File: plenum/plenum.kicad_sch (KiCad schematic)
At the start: 4 parts

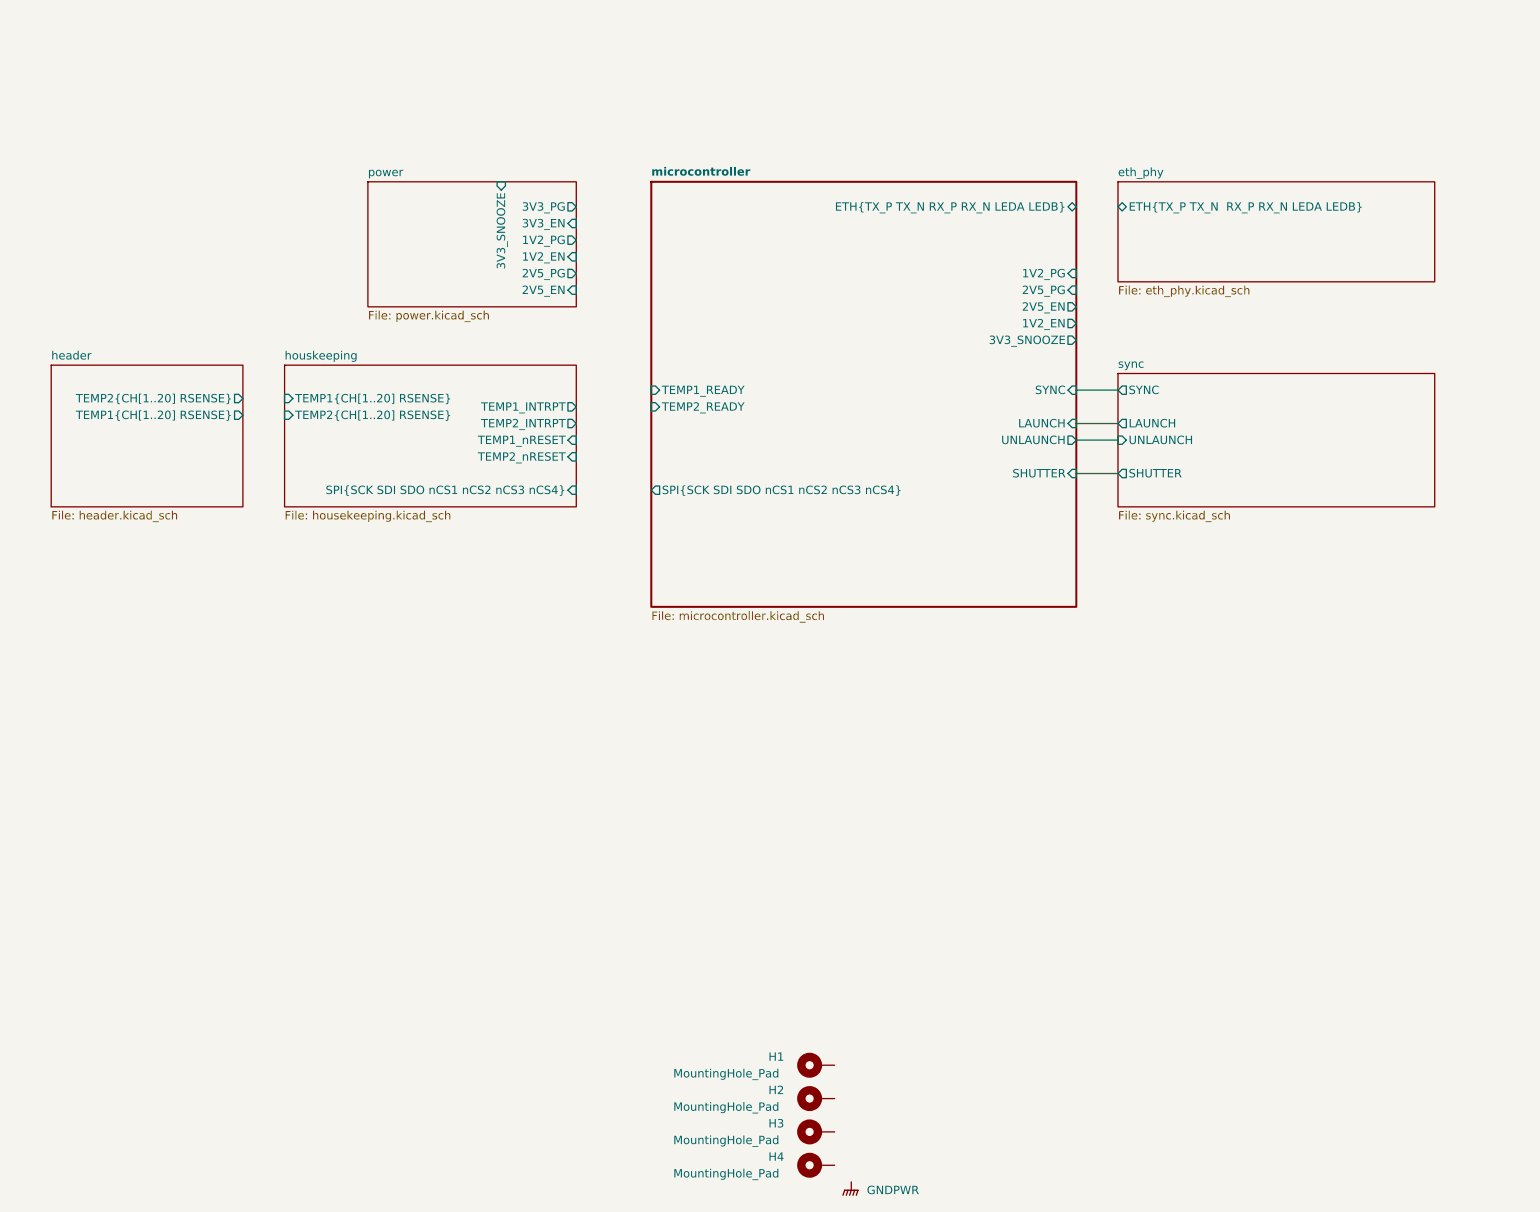
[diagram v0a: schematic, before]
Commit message: adding notes and BMI270 IMU to plenum
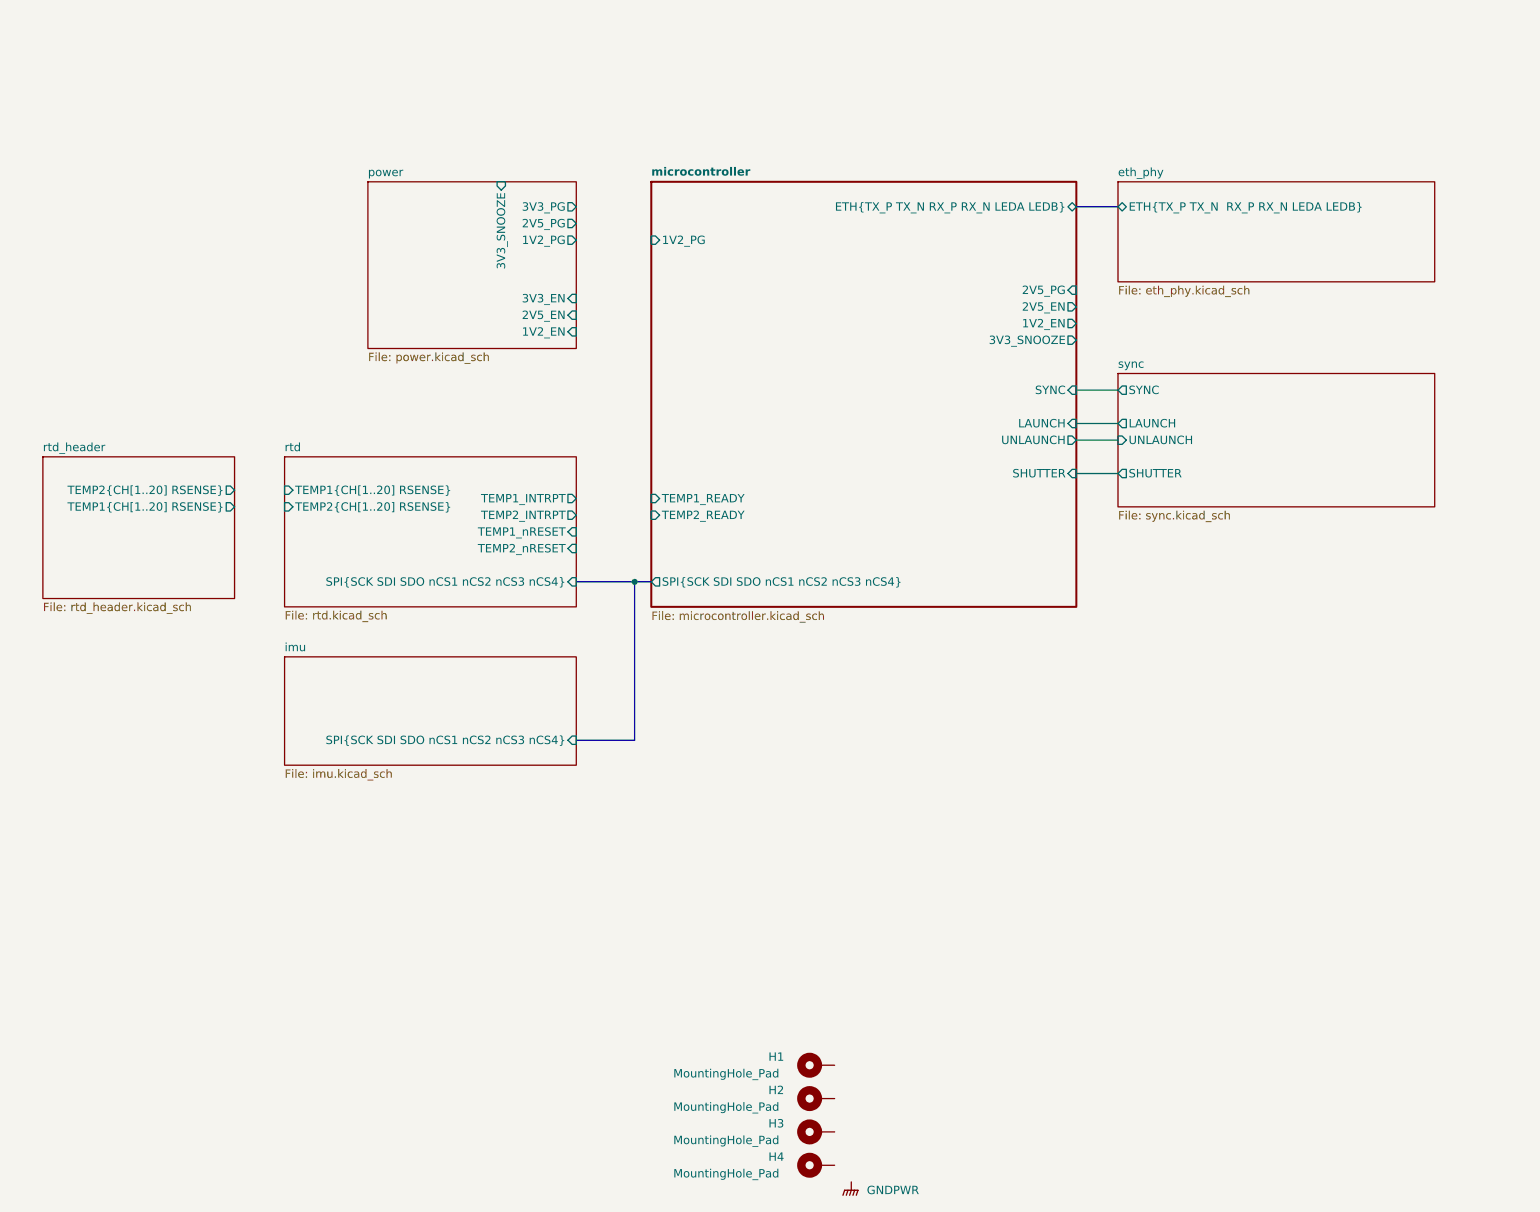
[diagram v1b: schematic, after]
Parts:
- H1, H2, H3, H4: footprint (none) -> MountingHole:MountingHole_3.2mm_M3_Pad
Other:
- sheet header renamed rtd_header
- sheet houskeeping renamed rtd
- added sheet imu (imu.kicad_sch)
- sheet rtd: file housekeeping.kicad_sch -> rtd.kicad_sch
- sheet rtd_header: file header.kicad_sch -> rtd_header.kicad_sch

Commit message: adding housekeeping board
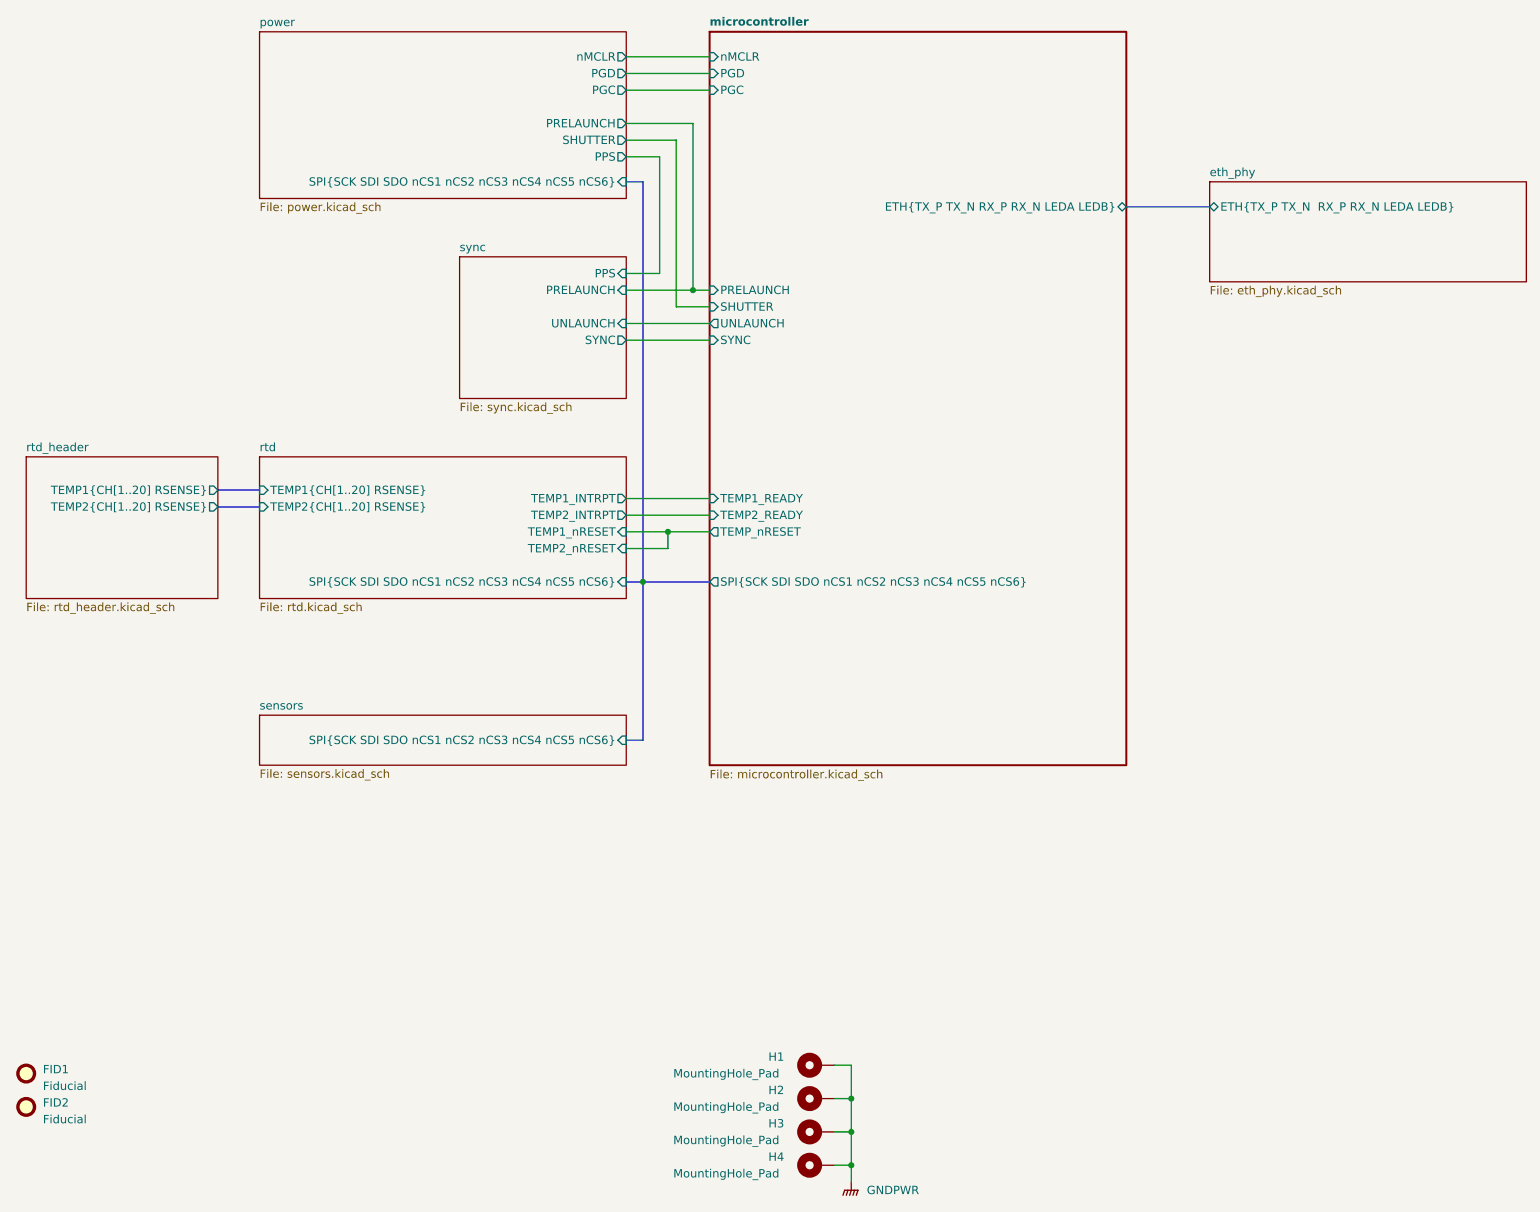
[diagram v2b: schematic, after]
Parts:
- added FID1, FID2: Fiducial, Fiducial:Fiducial_1mm_Mask2mm, symbol Mechanical:Fiducial
- H1, H2, H3, H4: footprint MountingHole:MountingHole_3.2mm_M3_Pad -> MountingHole:MountingHole_0.112in_Pad
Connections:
- net GNDPWR: now also H1.1, H2.1, H3.1, H4.1
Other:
- sheet imu renamed sensors
- sheet microcontroller ports: added PGC, PGD, PRELAUNCH, SPI{SCK SDI SDO nCS1 nCS2 nCS3 nCS4 nCS5 nCS6}, TEMP_nRESET, nMCLR; removed 1V2_EN, 1V2_PG, 2V5_EN, 2V5_PG, 3V3_SNOOZE, LAUNCH, SPI{SCK SDI SDO nCS1 nCS2 nCS3 nCS4}
- sheet power ports: added PGC, PGD, PPS, PRELAUNCH, SHUTTER, SPI{SCK SDI SDO nCS1 nCS2 nCS3 nCS4 nCS5 nCS6}, nMCLR; removed 1V2_EN, 1V2_PG, 2V5_EN, 2V5_PG, 3V3_EN, 3V3_PG, 3V3_SNOOZE
- sheet rtd ports: added SPI{SCK SDI SDO nCS1 nCS2 nCS3 nCS4 nCS5 nCS6}; removed SPI{SCK SDI SDO nCS1 nCS2 nCS3 nCS4}
- sheet sensors: file imu.kicad_sch -> sensors.kicad_sch
- sheet sensors ports: added SPI{SCK SDI SDO nCS1 nCS2 nCS3 nCS4 nCS5 nCS6}; removed SPI{SCK SDI SDO nCS1 nCS2 nCS3 nCS4}
- sheet sync ports: added PPS, PRELAUNCH; removed LAUNCH, SHUTTER
